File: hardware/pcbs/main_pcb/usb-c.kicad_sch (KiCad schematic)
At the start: 16 parts, among them J6 Conn_01x02, J7 USB_C_Receptacle_USB2.0_14P, U4 AMS1117-3.3, U6 CH340C

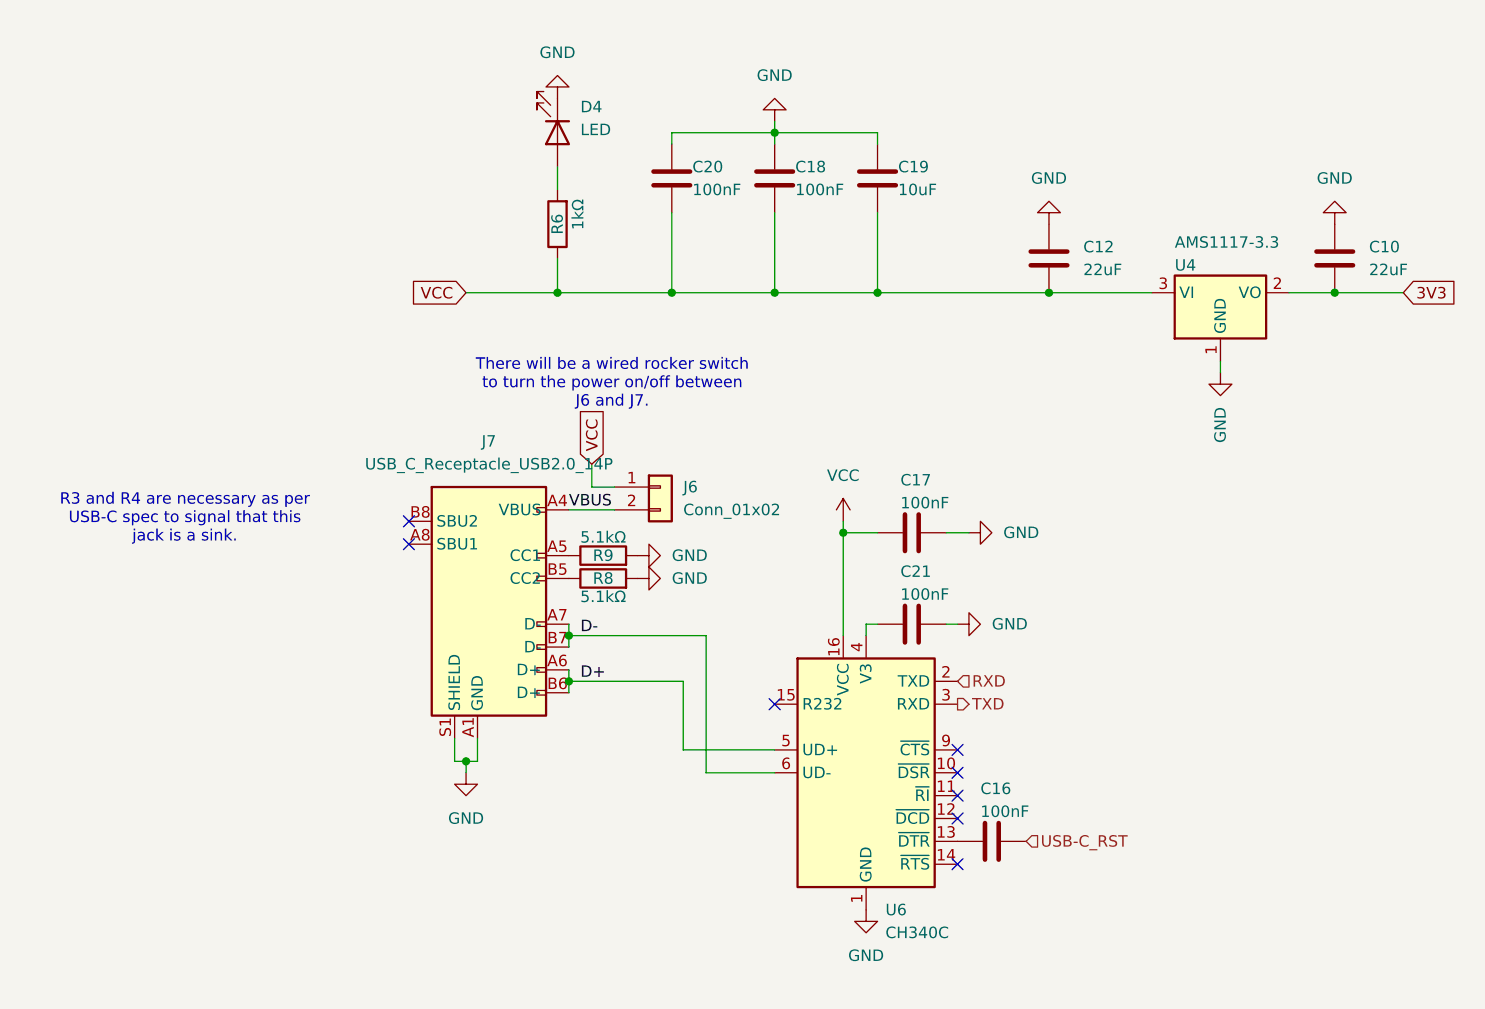
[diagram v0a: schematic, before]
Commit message: Maddie/main pcb schematic cleaning (#88)
* feat(main PCB): Reworks schematic

* feat(main PCB): Removes no longer used BL pin 01x02 header

* feat(main PCB): Fixes main PCB routing issue

* chore: Reworks main PCB schematic/PCB

* chore: Removes old csv file
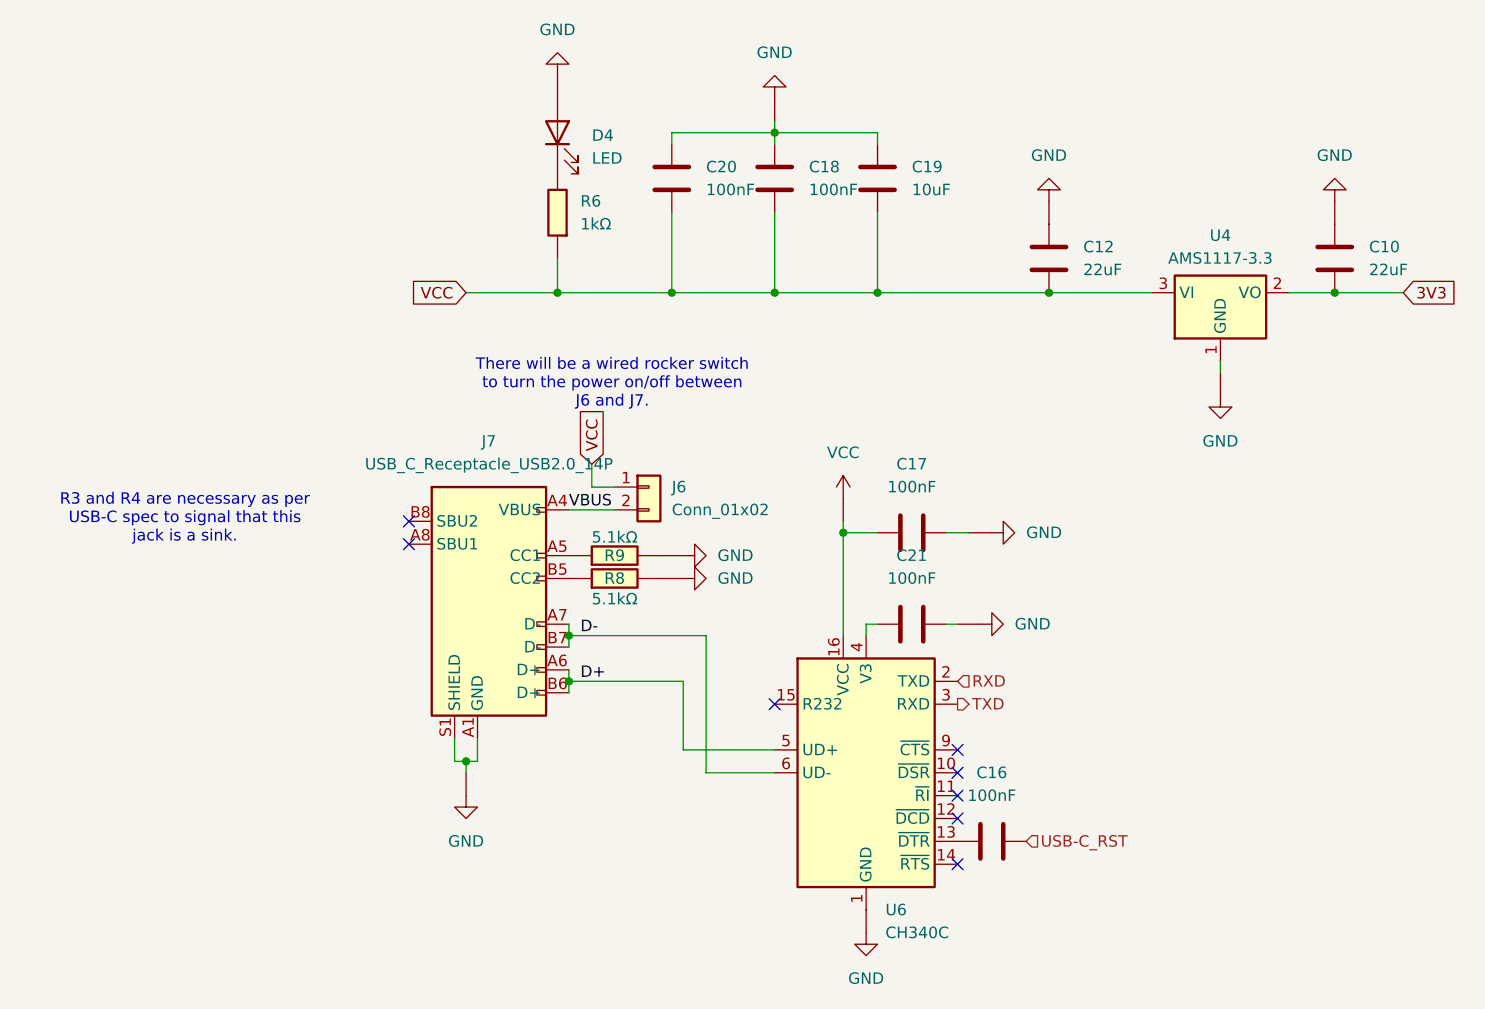
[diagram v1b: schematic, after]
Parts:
- C10, C12, C16, C17, C18, C19, C20, C21: symbol Device:C -> Lilybrary:Capacitor
- D4: symbol Device:LED -> Lilybrary:LED
- J6: symbol Connector_Generic:Conn_01x02 -> Lilybrary:Conn_01x02
- R6, R8, R9: symbol Device:R -> Lilybrary:Resistor
- U4: footprint Package_TO_SOT_SMD:SOT-223-3_TabPin2 -> Lilibrary:SOT-223-3_TabPin2_AMS1117; symbol Regulator_Linear:AMS1117-3.3 -> Lilybrary:AMS117-3.3
- U6: symbol Interface_USB:CH340C -> Lilybrary:CH340C
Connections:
- net GND: now also D4.2 (A); no longer D4.1 (K)
- net at R6.2: now also D4.1 (K); no longer D4.2 (A)
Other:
- company: (none) -> Lily's Pad
- title: (none) -> Main PCB: USB-C
- moved on the sheet: D4, J6

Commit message: fix: swaps CH340C because KiCad keeps swapping it for the default one (#127)
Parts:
- U6: footprint Package_SO:SOIC-16_3.9x9.9mm_P1.27mm -> Lilibrary:SOP-16_CH340C
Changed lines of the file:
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@@
 			)
 		)
-		(property "Footprint" "Package_SO:SOIC-16_3.9x9.9mm_P1.27mm"
+		(property "Footprint" "Lilibrary:SOP-16_CH340C"
 			(at 158.75 125.73 0)
 			(effects
